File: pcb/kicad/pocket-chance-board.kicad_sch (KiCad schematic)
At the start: 123 parts, among them J1 SWD, J2 USB4085-GF-A, J3 LiPo JST-PH 2.0mm (pin 1 = + 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, J4 LCD 1.54in ST7789 module, JST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, J5 Speaker JST-PH, J6 microSD Molex 104031-0811, J7 STEMMA QT, J8 Expansion, Q1 FS8205A, Q2 DMG2305UX, SW1 BOOT, SW10 JOY LEFT, SW11 JOY RIGHT, SW12 JOY PRESS, SW2 RESET, SW3 POWER PCM12, SW4 A PTS125SM43SMTR2LFS, SW5 B PTS125SM43SMTR2LFS, SW6 X PTS125SM43SMTR2LFS, SW7 Y PTS125SM43SMTR2LFS, SW8 JOY UP, SW9 JOY DOWN, U1 RP2350A, U10 LSM6DSOXTR, U11 RM2, U2 W25Q128JVSIQ, U3 APS6404L-3SQR-SN, U4 USBLC6-2SC6, U5 BQ24074RGTR, U6 TPS63001DRCR, U7 DW01A, U8 PAM8302AADCR, U9 DS3231MZ+, Y1 12MHz ABM8-272-T3

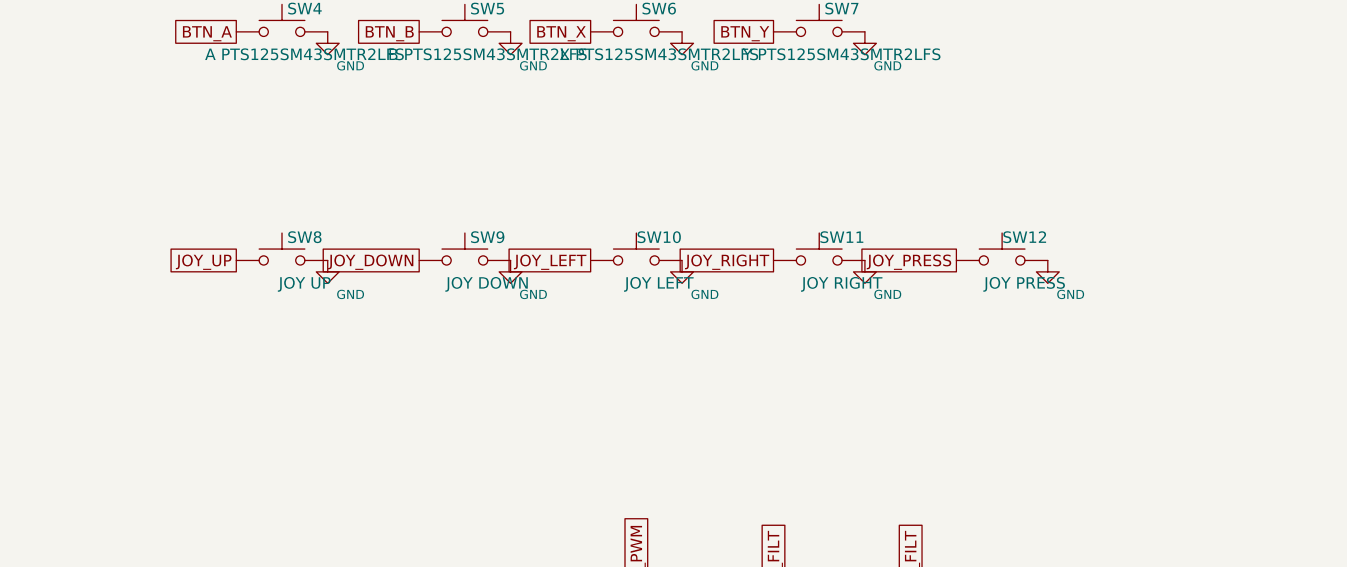
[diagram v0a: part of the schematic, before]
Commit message: Fix the direction-pad edit; schematic regenerated (ERC: 0 errors, 1 expected warning)
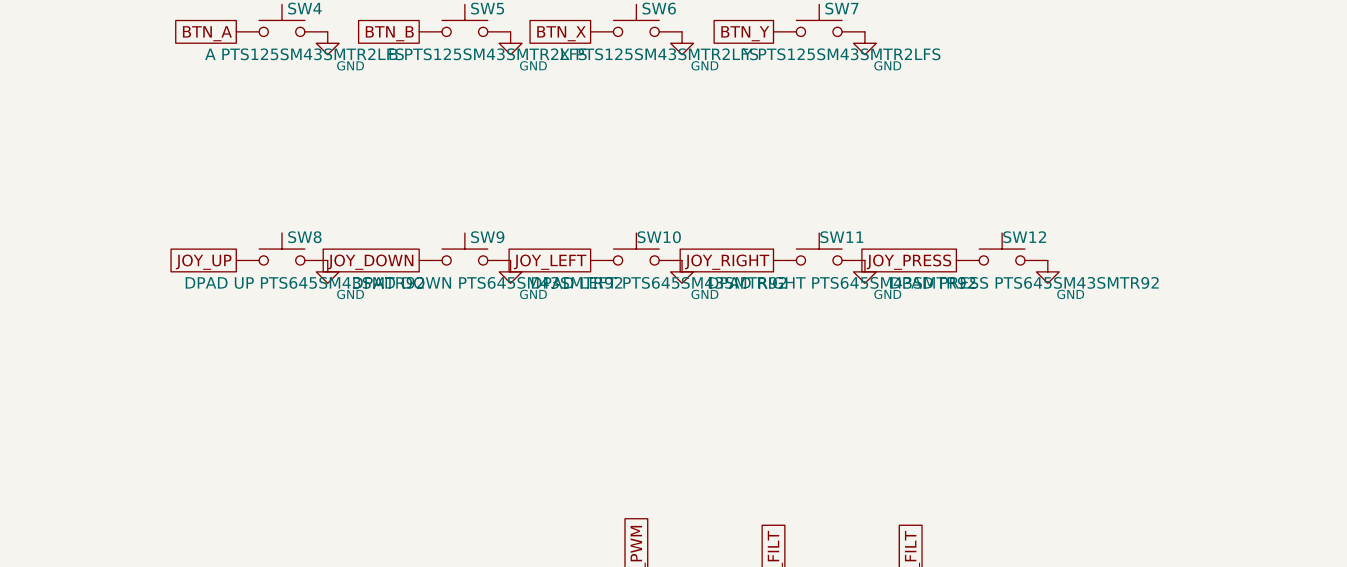
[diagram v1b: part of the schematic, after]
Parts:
- L1: footprint Inductor_SMD:L_0805_2012Metric -> pcb_custom:AOTA-B201610S
- SW10: value JOY LEFT -> DPAD LEFT PTS645SM43SMTR92; footprint pcb_custom:Alps_SKRHABE010 -> Button_Switch_SMD:SW_SPST_PTS645Sx43SMTR92
- SW11: value JOY RIGHT -> DPAD RIGHT PTS645SM43SMTR92; footprint pcb_custom:Alps_SKRHABE010 -> Button_Switch_SMD:SW_SPST_PTS645Sx43SMTR92
- SW12: value JOY PRESS -> DPAD PRESS PTS645SM43SMTR92; footprint pcb_custom:Alps_SKRHABE010 -> Button_Switch_SMD:SW_SPST_PTS645Sx43SMTR92
- SW8: value JOY UP -> DPAD UP PTS645SM43SMTR92; footprint pcb_custom:Alps_SKRHABE010 -> Button_Switch_SMD:SW_SPST_PTS645Sx43SMTR92
- SW9: value JOY DOWN -> DPAD DOWN PTS645SM43SMTR92; footprint pcb_custom:Alps_SKRHABE010 -> Button_Switch_SMD:SW_SPST_PTS645Sx43SMTR92
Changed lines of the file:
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@@
 			)
 		)
-		(property "Footprint" "Inductor_SMD:L_0805_2012Metric"
+		(property "Footprint" "pcb_custom:AOTA-B201610S"
 			(at 129.54 110.49 0)
 			(effects
@@
 			)
 		)
-		(property "Value" "JOY UP"
+		(property "Value" "DPAD UP PTS645SM43SMTR92"
 			(at 482.6 157.48 0)
 			(effects
@@
 			)
 		)
-		(property "Footprint" "pcb_custom:Alps_SKRHABE010"
+		(property "Footprint" "Button_Switch_SMD:SW_SPST_PTS645Sx43SMTR92"
 			(at 480.06 154.94 0)
 			(effects
@@
 			)
 		)
-		(property "Value" "JOY DOWN"
+		(property "Value" "DPAD DOWN PTS645SM43SMTR92"
 			(at 502.92 157.48 0)
 			(effects
@@
 			)
 		)
-		(property "Footprint" "pcb_custom:Alps_SKRHABE010"
+		(property "Footprint" "Button_Switch_SMD:SW_SPST_PTS645Sx43SMTR92"
 			(at 500.38 154.94 0)
 			(effects
@@
 			)
 		)
-		(property "Value" "JOY LEFT"
+		(property "Value" "DPAD LEFT PTS645SM43SMTR92"
 			(at 521.97 157.48 0)
 			(effects
@@
 			)
 		)
-		(property "Footprint" "pcb_custom:Alps_SKRHABE010"
+		(property "Footprint" "Button_Switch_SMD:SW_SPST_PTS645Sx43SMTR92"
 			(at 519.43 154.94 0)
 			(effects
@@
 			)
 		)
-		(property "Value" "JOY RIGHT"
+		(property "Value" "DPAD RIGHT PTS645SM43SMTR92"
 			(at 542.29 157.48 0)
 			(effects
@@
 			)
 		)
-		(property "Footprint" "pcb_custom:Alps_SKRHABE010"
+		(property "Footprint" "Button_Switch_SMD:SW_SPST_PTS645Sx43SMTR92"
 			(at 539.75 154.94 0)
 			(effects
@@
 			)
 		)
-		(property "Value" "JOY PRESS"
+		(property "Value" "DPAD PRESS PTS645SM43SMTR92"
 			(at 562.61 157.48 0)
 			(effects
@@
 			)
 		)
-		(property "Footprint" "pcb_custom:Alps_SKRHABE010"
+		(property "Footprint" "Button_Switch_SMD:SW_SPST_PTS645Sx43SMTR92"
 			(at 560.07 154.94 0)
 			(effects

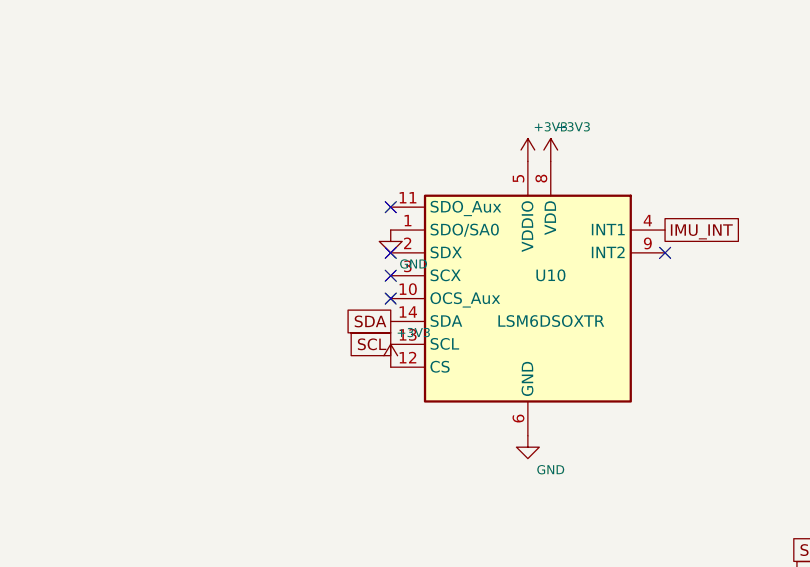
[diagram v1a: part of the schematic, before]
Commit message: IMU: pin map and unused-pin handling from the ST datasheet; REVIEW-1 item 6 closed
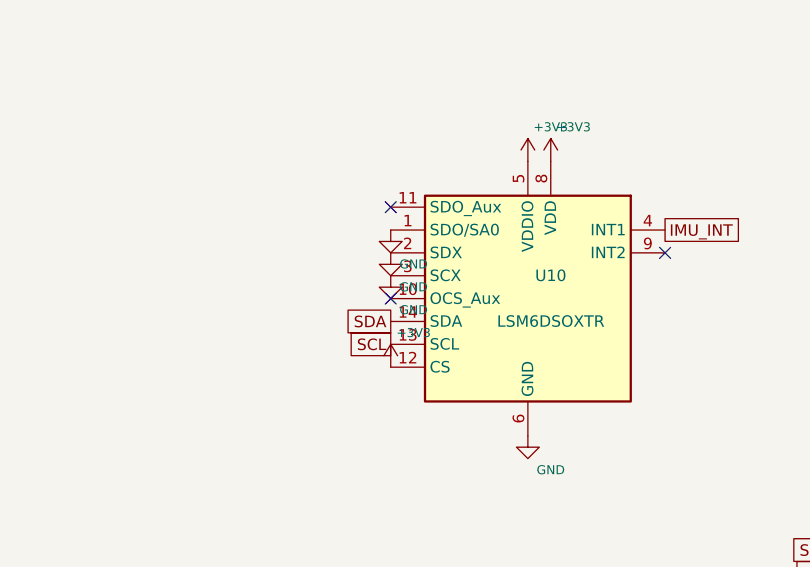
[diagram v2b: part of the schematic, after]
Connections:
- net GND: now also U10.2 (SDX), U10.3 (SCX)
- no-connect marks 20 -> 18

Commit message: Phase 5: charger footprint with TI's 1.68 mm thermal pad and vias
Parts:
- U5: footprint Package_DFN_QFN:VQFN-16-1EP_3x3mm_P0.5mm_EP1.6x1.6mm -> Package_DFN_QFN:VQFN-16-1EP_3x3mm_P0.5mm_EP1.68x1.68mm_ThermalVias
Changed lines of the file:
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@@
 			)
 		)
-		(property "Footprint" "Package_DFN_QFN:VQFN-16-1EP_3x3mm_P0.5mm_EP1.6x1.6mm"
+		(property "Footprint" "Package_DFN_QFN:VQFN-16-1EP_3x3mm_P0.5mm_EP1.68x1.68mm_ThermalVias"
 			(at 299.72 180.34 0)
 			(effects
